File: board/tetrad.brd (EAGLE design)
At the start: 100 x 100 mm, 89 parts, among them Q1 40V, U2 RADIO-ESP32_DEVKIT, U3 R-78E5.0-1.0

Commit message: started work on v1.1
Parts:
- Q1: value 40V -> FET-PCH-TO252
- Q10, Q11, Q12, Q2, Q3, Q4, Q5, Q6, Q7, Q8, Q9: value (none) -> FET-NCH-SOT23
- R1, R7: value 2k -> 1k
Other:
- board text added: "tetrad 191101 v1.0"
- board text removed: "hexad 191101 v1.0"
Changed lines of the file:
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@@
 <wire x1="0.5" y1="28.815" x2="2.5" y2="28.815" width="0.5" layer="52"/>
 <rectangle x1="87.63" y1="29.845" x2="95.25" y2="33.655" layer="51"/>
-<text x="87.884" y="34.036" size="0.9144" layer="51" ratio="20">hexad
+<text x="87.884" y="34.036" size="0.9144" layer="51" ratio="20">tetrad
 191101
 v1.0</text>
@@
 <attribute name="VALUE" x="27.04" y="24.215" size="0.9144" layer="27" ratio="20"/>
 </element>
-<element name="Q1" library="holla" package="TO252" value="40V" x="14.635" y="26.715" smashed="yes">
+<element name="Q1" library="holla" package="TO252" value="FET-PCH-TO252" x="14.635" y="26.715" smashed="yes">
 <attribute name="NAME" x="11.475" y="33.117" size="0.9144" layer="25" ratio="20"/>
 <attribute name="VALUE" x="19.715" y="24.175" size="0.9144" layer="27" ratio="20" rot="R90"/>
@@
 <attribute name="VALUE" x="24.666" y="11.095" size="0.9144" layer="27" ratio="20" rot="R90" align="top-center"/>
 </element>
-<element name="Q12" library="holla" package="SOT23-3" value="" x="17.285" y="11.095" smashed="yes" rot="R90">
+<element name="Q12" library="holla" package="SOT23-3" value="FET-NCH-SOT23" x="17.285" y="11.095" smashed="yes" rot="R90">
 <attribute name="VALUE" x="14.0846" y="9.6726" size="1.27" layer="27" ratio="10" rot="R90"/>
 <attribute name="NAME" x="17.78" y="13.335" size="0.9144" layer="25" ratio="20" rot="R90"/>
 </element>
-<element name="Q11" library="holla" package="SOT23-3" value="" x="12.92" y="11.095" smashed="yes" rot="R90">
+<element name="Q11" library="holla" package="SOT23-3" value="FET-NCH-SOT23" x="12.92" y="11.095" smashed="yes" rot="R90">
 <attribute name="VALUE" x="9.7196" y="9.6726" size="1.27" layer="27" ratio="10" rot="R90"/>
 <attribute name="NAME" x="13.335" y="13.335" size="0.9144" layer="25" ratio="20" rot="R90"/>
@@
 <attribute name="VALUE" x="38.481" y="11.43" size="0.9144" layer="27" ratio="20" rot="R90" align="top-center"/>
 </element>
-<element name="Q3" library="holla" package="SOT23-3" value="" x="33.655" y="11.43" smashed="yes" rot="R90">
+<element name="Q3" library="holla" package="SOT23-3" value="FET-NCH-SOT23" x="33.655" y="11.43" smashed="yes" rot="R90">
 <attribute name="VALUE" x="30.4546" y="10.0076" size="1.27" layer="27" ratio="10" rot="R90"/>
 <attribute name="NAME" x="34.036" y="13.335" size="0.9144" layer="25" ratio="20" rot="R90"/>
 </element>
-<element name="Q2" library="holla" package="SOT23-3" value="" x="29.21" y="11.43" smashed="yes" rot="R90">
+<element name="Q2" library="holla" package="SOT23-3" value="FET-NCH-SOT23" x="29.21" y="11.43" smashed="yes" rot="R90">
 <attribute name="VALUE" x="26.0096" y="10.0076" size="1.27" layer="27" ratio="10" rot="R90"/>
 <attribute name="NAME" x="29.591" y="13.335" size="0.9144" layer="25" ratio="20" rot="R90"/>
@@
 <attribute name="VALUE" x="54.991" y="11.43" size="0.9144" layer="27" ratio="20" rot="R90" align="top-center"/>
 </element>
-<element name="Q5" library="holla" package="SOT23-3" value="" x="50.165" y="11.43" smashed="yes" rot="R90">
+<element name="Q5" library="holla" package="SOT23-3" value="FET-NCH-SOT23" x="50.165" y="11.43" smashed="yes" rot="R90">
 <attribute name="VALUE" x="46.9646" y="10.0076" size="1.27" layer="27" ratio="10" rot="R90"/>
 <attribute name="NAME" x="50.8" y="13.335" size="0.9144" layer="25" ratio="20" rot="R90"/>
 </element>
-<element name="Q4" library="holla" package="SOT23-3" value="" x="45.72" y="11.43" smashed="yes" rot="R90">
+<element name="Q4" library="holla" package="SOT23-3" value="FET-NCH-SOT23" x="45.72" y="11.43" smashed="yes" rot="R90">
 <attribute name="VALUE" x="42.5196" y="10.0076" size="1.27" layer="27" ratio="10" rot="R90"/>
 <attribute name="NAME" x="46.355" y="13.335" size="0.9144" layer="25" ratio="20" rot="R90"/>
@@
 <attribute name="VALUE" x="71.501" y="11.43" size="0.9144" layer="27" ratio="20" rot="R90" align="top-center"/>
 </element>
-<element name="Q7" library="holla" package="SOT23-3" value="" x="66.675" y="11.43" smashed="yes" rot="R90">
+<element name="Q7" library="holla" package="SOT23-3" value="FET-NCH-SOT23" x="66.675" y="11.43" smashed="yes" rot="R90">
 <attribute name="VALUE" x="63.4746" y="10.0076" size="1.27" layer="27" ratio="10" rot="R90"/>
 <attribute name="NAME" x="67.31" y="13.335" size="0.9144" layer="25" ratio="20" rot="R90"/>
 </element>
-<element name="Q6" library="holla" package="SOT23-3" value="" x="62.23" y="11.43" smashed="yes" rot="R90">
+<element name="Q6" library="holla" package="SOT23-3" value="FET-NCH-SOT23" x="62.23" y="11.43" smashed="yes" rot="R90">
 <attribute name="VALUE" x="59.0296" y="10.0076" size="1.27" layer="27" ratio="10" rot="R90"/>
 <attribute name="NAME" x="62.865" y="13.335" size="0.9144" layer="25" ratio="20" rot="R90"/>
@@
 <attribute name="VALUE" x="74.041" y="11.43" size="0.9144" layer="27" ratio="20" rot="R90" align="top-center"/>
 </element>
-<element name="R7" library="holla" package="R-0603" value="2k" x="59.905" y="82.735" smashed="yes" rot="R180">
+<element name="R7" library="holla" package="R-0603" value="1k" x="59.905" y="82.735" smashed="yes" rot="R180">
 <attribute name="NAME" x="59.905" y="84.767" size="0.9144" layer="25" ratio="20" rot="R180" align="bottom-center"/>
 <attribute name="VALUE" x="59.905" y="83.751" size="0.9144" layer="27" ratio="20" rot="R180" align="top-center"/>
 </element>
-<element name="R1" library="holla" package="R-0603" value="2k" x="59.69" y="90.805" smashed="yes" rot="R180">
+<element name="R1" library="holla" package="R-0603" value="1k" x="59.69" y="90.805" smashed="yes" rot="R180">
 <attribute name="NAME" x="59.69" y="92.837" size="0.9144" layer="25" ratio="20" rot="R180" align="bottom-center"/>
 <attribute name="VALUE" x="59.69" y="91.821" size="0.9144" layer="27" ratio="20" rot="R180" align="top-center"/>
@@
 <attribute name="VALUE" x="89.464" y="11.425" size="0.9144" layer="27" ratio="20" rot="R270" align="top-center"/>
 </element>
-<element name="Q8" library="holla" package="SOT23-3" value="" x="82.55" y="11.43" smashed="yes" rot="R90">
+<element name="Q8" library="holla" package="SOT23-3" value="FET-NCH-SOT23" x="82.55" y="11.43" smashed="yes" rot="R90">
 <attribute name="VALUE" x="79.3496" y="10.0076" size="1.27" layer="27" ratio="10" rot="R90"/>
 <attribute name="NAME" x="83.185" y="13.335" size="0.9144" layer="25" ratio="20" rot="R90"/>
 </element>
-<element name="Q10" library="holla" package="SOT23-3" value="" x="78.115" y="11.425" smashed="yes" rot="R90">
+<element name="Q10" library="holla" package="SOT23-3" value="FET-NCH-SOT23" x="78.115" y="11.425" smashed="yes" rot="R90">
 <attribute name="VALUE" x="74.9146" y="10.0026" size="1.27" layer="27" ratio="10" rot="R90"/>
 <attribute name="NAME" x="78.74" y="13.335" size="0.9144" layer="25" ratio="20" rot="R90"/>
@@
 <attribute name="VALUE" x="91.829" y="11.425" size="0.9144" layer="27" ratio="20" rot="R270" align="top-center"/>
 </element>
-<element name="Q9" library="holla" package="SOT23-3" value="" x="86.995" y="11.43" smashed="yes" rot="R90">
+<element name="Q9" library="holla" package="SOT23-3" value="FET-NCH-SOT23" x="86.995" y="11.43" smashed="yes" rot="R90">
 <attribute name="VALUE" x="83.7946" y="10.0076" size="1.27" layer="27" ratio="10" rot="R90"/>
 <attribute name="NAME" x="87.63" y="13.335" size="0.9144" layer="25" ratio="20" rot="R90"/>

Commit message: updated schematic
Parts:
- U1: value (none) -> IO-MCP23017SO
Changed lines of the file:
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@@
 <attribute name="VALUE" x="96.085" y="67.445" size="1.27" layer="27" rot="R90"/>
 </element>
-<element name="U1" library="holla" package="SO28W" value="" x="25" y="80" smashed="yes">
+<element name="U1" library="holla" package="SO28W" value="IO-MCP23017SO" x="25" y="80" smashed="yes">
 <attribute name="OC_NEWARK" value="31K2958" x="25" y="80" size="1.778" layer="27" display="off"/>
 <attribute name="MF" value="MICROCHIP" x="25" y="80" size="1.778" layer="27" display="off"/>

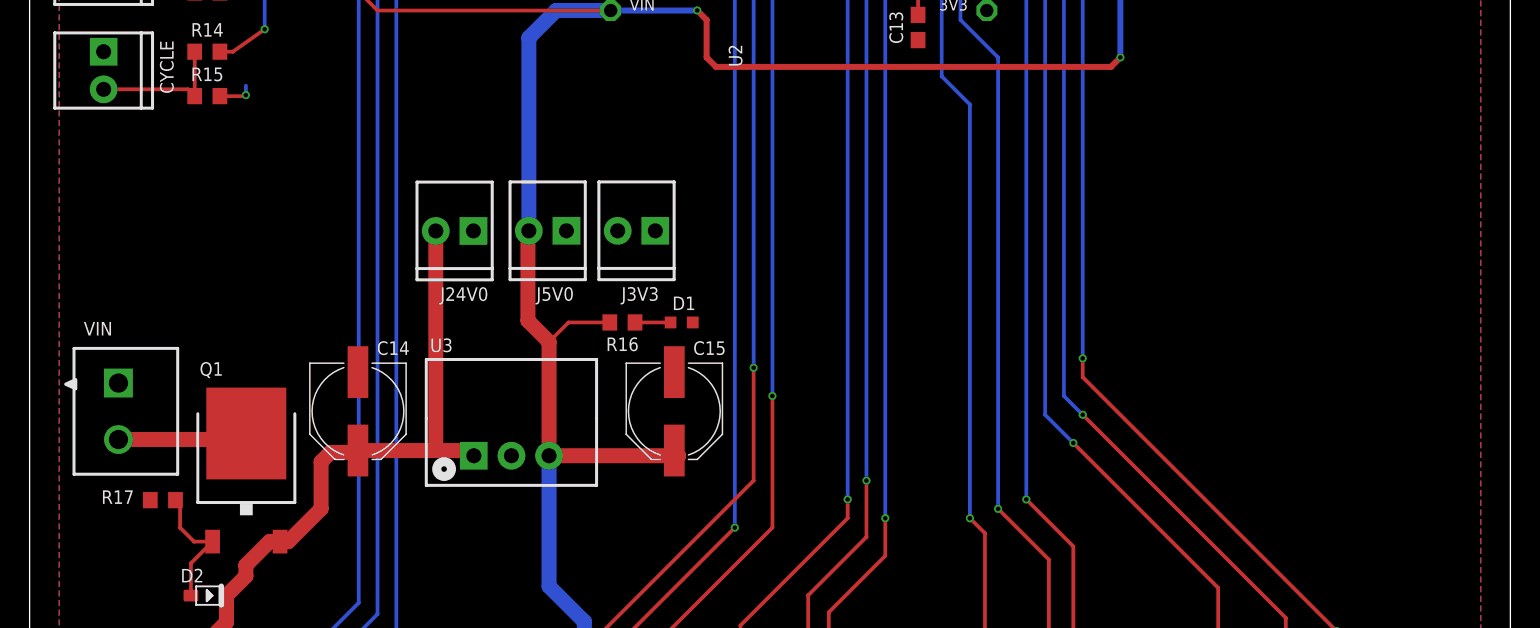
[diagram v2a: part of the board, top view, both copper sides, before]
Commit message: started fixing board mistakes
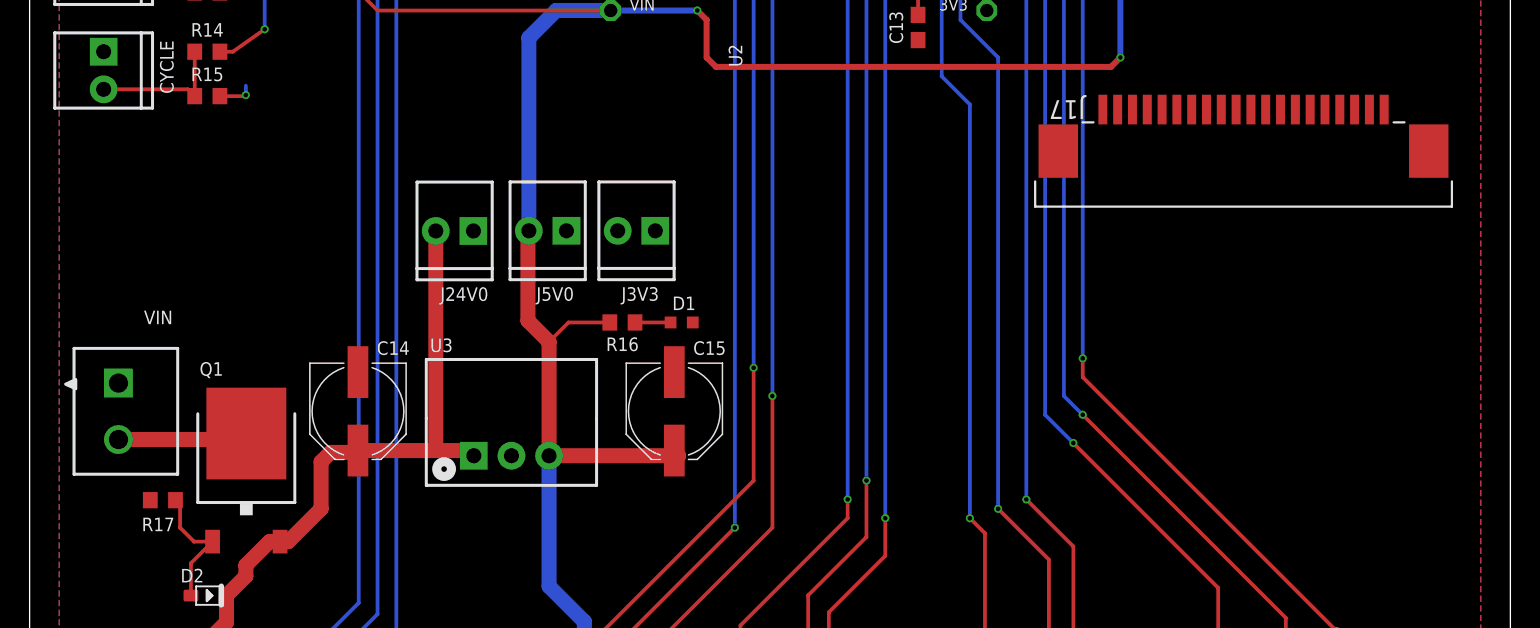
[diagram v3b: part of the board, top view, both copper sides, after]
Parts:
- added J17: (no value), holla:CON20_SMT-RA_FCC-FPC2
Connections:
- new net AUDIO: J17.9
- new net CS_DISPLAY: J17.6
- new net INT_DISPLAY: J17.7
- new net PD_DISPLAY: J17.8
- net 3V3: now also J17.1, J17.17, J17.18
- net GND: now also J17.19, J17.2, J17.20
- net MISO: now also J17.4
- net MOSI: now also J17.5
- net SCK: now also J17.3
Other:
- board text added: "8-24VDC"

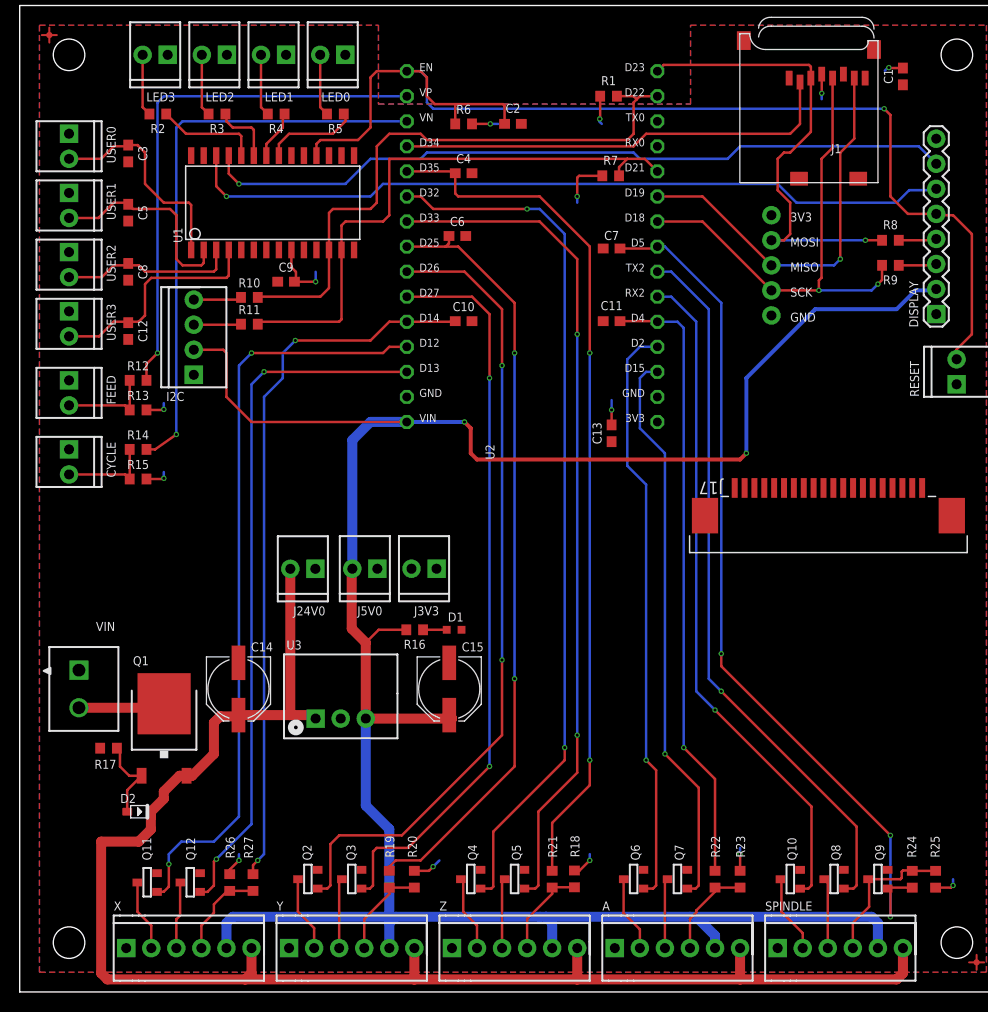
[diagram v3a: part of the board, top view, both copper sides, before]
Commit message: beefed up 24v0 traces
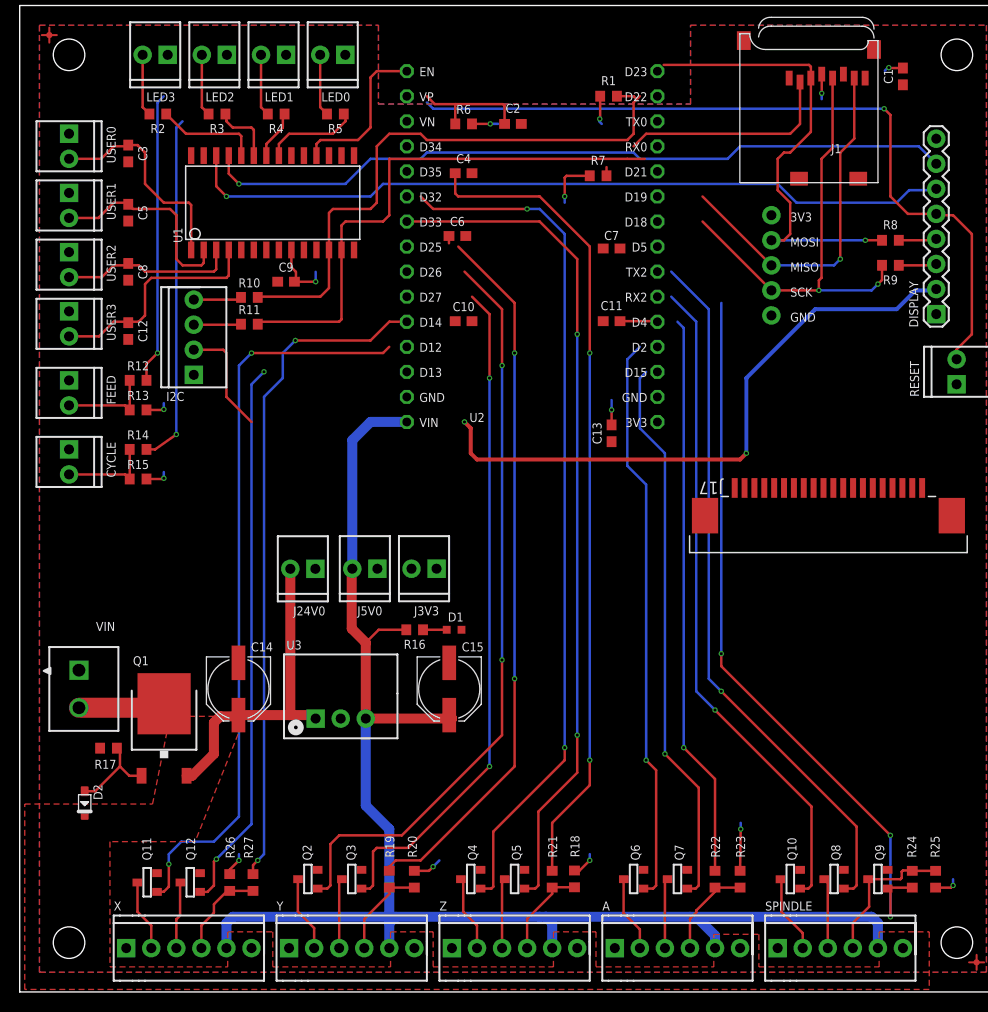
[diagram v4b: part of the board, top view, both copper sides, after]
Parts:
- moved D2 5.58 mm to (6.59, 19.1), turned to 270 degrees
- moved R7 1.27 mm to (58.6, 82.7)
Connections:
- net CS_SD: now also U2.D25; no longer U2.D34
- net Y_LIMIT: now also U2.D34; no longer U2.D25
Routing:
- net 24V0: track 156.6 -> 32.5 mm
- net FEED_HOLD: track 54.2 -> 29.5 mm
- net CS_SD: track 45.1 -> 22.1 mm
- net CYCLE_START: track 58.2 -> 35.5 mm
- net 5V0: track 248.6 -> 227.0 mm
- net X_STEP: track 70.3 -> 55.9 mm
- net SPINDLE_ENABLE: track 87.5 -> 74.8 mm
- net RESET: track 116.5 -> 107.4 mm
- net Y_STEP: track 75.1 -> 68.5 mm
- net Y_DIR: track 82.0 -> 76.1 mm
- net Y_LIMIT: track 78.8 -> 73.1 mm
- net X_LIMIT: track 72.9 -> 68.0 mm
- net Z_LIMIT: track 87.8 -> 83.0 mm
- net SCK: track 49.7 -> 45.1 mm
- net MISO: track 40.6 -> 36.1 mm
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- added copper zone on layer 1, net 24V0
